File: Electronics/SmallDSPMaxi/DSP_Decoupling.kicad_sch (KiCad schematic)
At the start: 27 parts

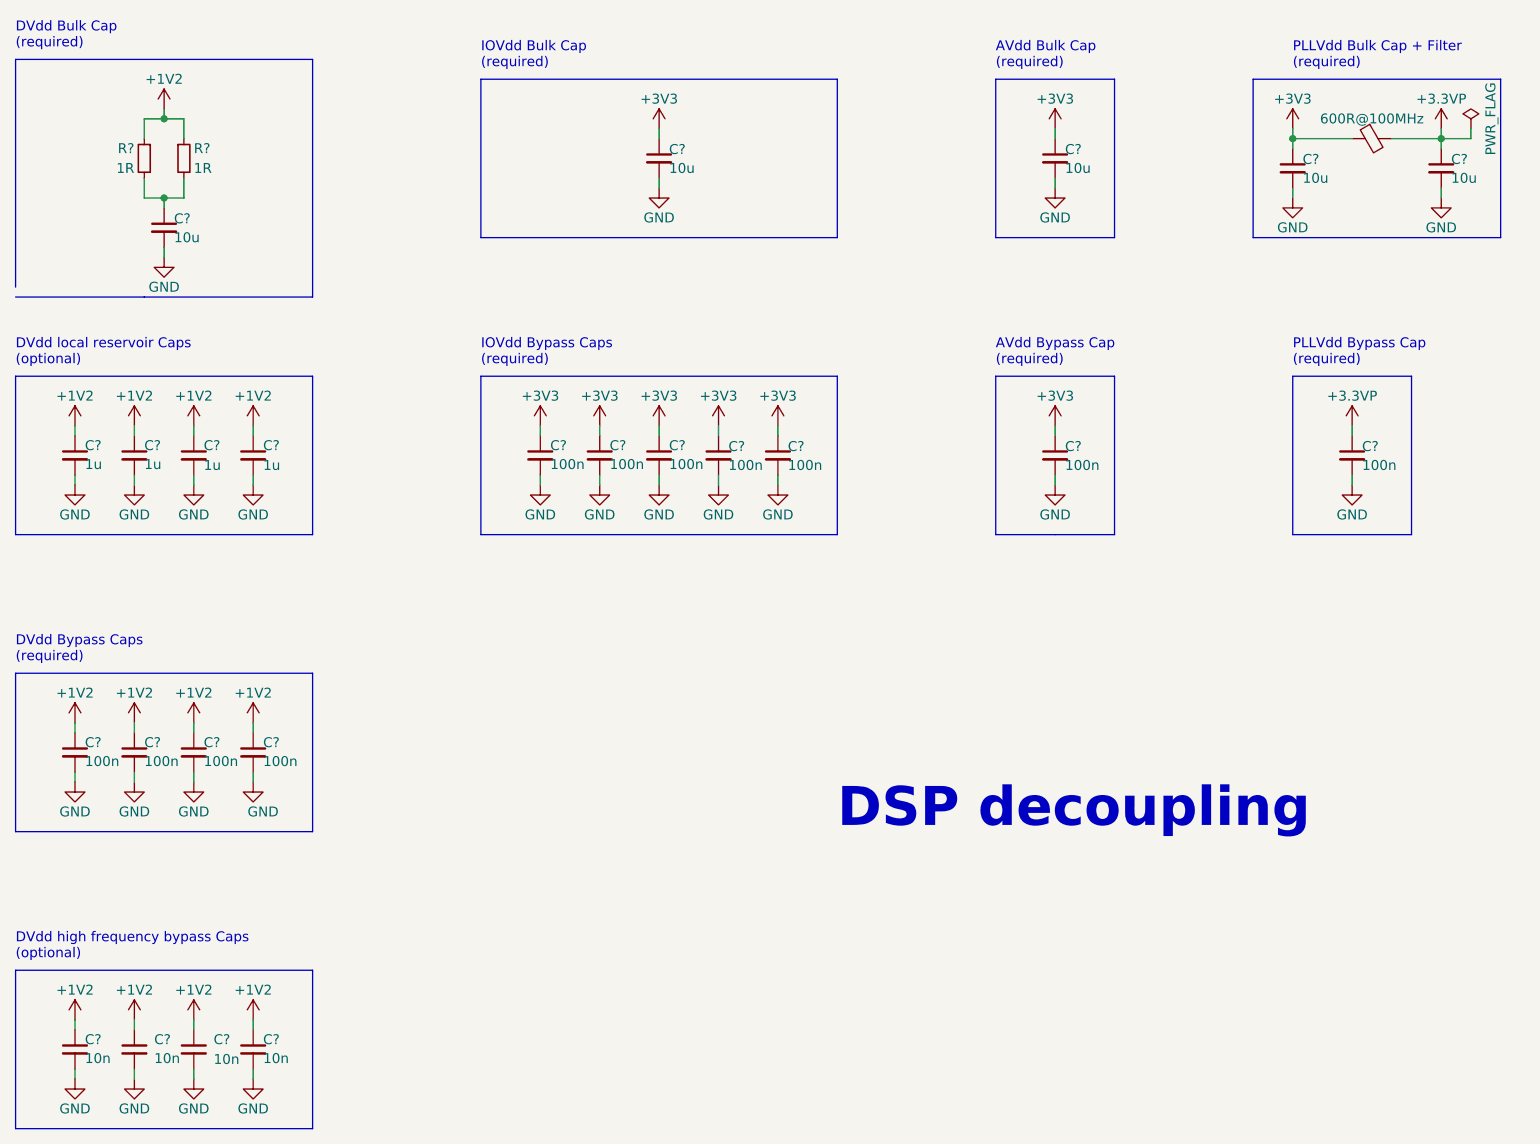
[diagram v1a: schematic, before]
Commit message: Adds AES17 measurements for rev1 of maxi. adds first iteration of maxi firmware. prototype now functional. adds mechanical information such as pcb 3d models and datasheets for psu and power switch, -connector.
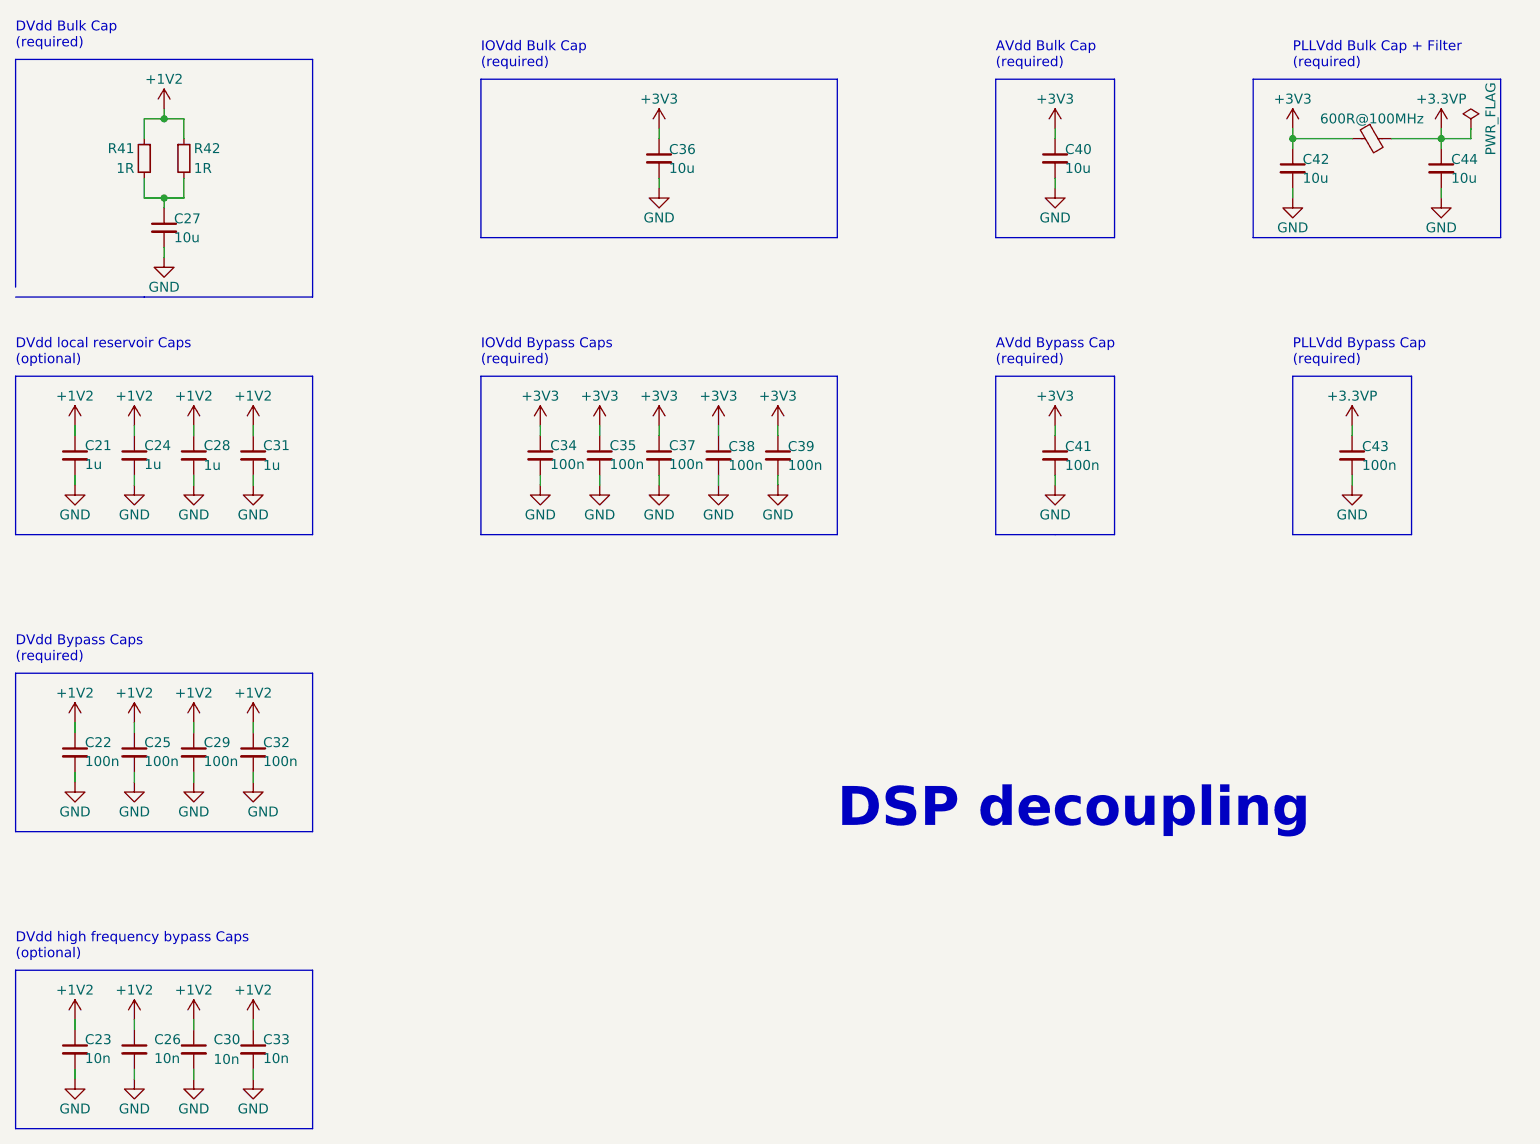
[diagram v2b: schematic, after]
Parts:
- gave numbers to parts that had none: 27
